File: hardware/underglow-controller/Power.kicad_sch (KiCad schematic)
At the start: 12 parts, among them U6 BD33C0AWFP-CE2

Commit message: almost done picking components i think
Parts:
- added D5: RB496EA, Package_TO_SOT_SMD:SOT-23-5, symbol ConeCodes:RB496EA
- gave numbers to parts that had none: 1
- renumbered C58 to C57, C57 to C58, R44 to R42, R40 to R43, R41 to R44, R42 to R45, R43 to R46
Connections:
- net IGNITION: now also D5.1 (A), D5.5 (K)
- net VBATT: now also D5.3 (A), D5.4 (K)
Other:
- moved on the sheet: D6
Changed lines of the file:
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@@
   (junction (at 57.15 76.2) (diameter 0) (color 0 0 0 0)
   )
-  (junction (at 35.56 76.2) (diameter 0) (color 0 0 0 0)
+  (junction (at 37.465 76.2) (diameter 0) (color 0 0 0 0)
   )
   (junction (at 81.915 77.47) (diameter 0) (color 0 0 0 0)
@@
     (stroke (width 0) (type default) (color 0 0 0 0))
   )
-  (wire (pts (xy 29.21 76.2) (xy 35.56 76.2))
+  (wire (pts (xy 33.02 76.2) (xy 37.465 76.2))
     (stroke (width 0) (type default) (color 0 0 0 0))
   )
@@
     (stroke (width 0) (type default) (color 0 0 0 0))
   )
-  (wire (pts (xy 35.56 76.2) (xy 57.15 76.2))
-    (stroke (width 0) (type default) (color 0 0 0 0))
-  )
   (wire (pts (xy 64.77 77.47) (xy 81.915 77.47))
     (stroke (width 0) (type default) (color 0 0 0 0))
@@
     (stroke (width 0) (type default) (color 0 0 0 0))
   )
-  (wire (pts (xy 34.29 71.12) (xy 53.34 71.12))
+  (wire (pts (xy 33.02 71.12) (xy 53.34 71.12))
     (stroke (width 0) (type default) (color 0 0 0 0))
   )
@@
     (stroke (width 0) (type default) (color 0 0 0 0))
   )
-  (wire (pts (xy 35.56 81.28) (xy 35.56 83.82))
+  (wire (pts (xy 37.465 81.28) (xy 37.465 83.82))
     (stroke (width 0) (type default) (color 0 0 0 0))
   )
@@
   )
   (wire (pts (xy 99.695 77.47) (xy 107.95 77.47))
+    (stroke (width 0) (type default) (color 0 0 0 0))
+  )
+  (wire (pts (xy 37.465 76.2) (xy 57.15 76.2))
     (stroke (width 0) (type default) (color 0 0 0 0))
   )
@@
     (effects (font (size 1.27 1.27)) (justify left bottom))
   )
-  (hierarchical_label "IGNITION" (shape input) (at 34.29 71.12 180)
+  (hierarchical_label "IGNITION" (shape input) (at 22.86 71.12 180)
     (effects (font (size 1.27 1.27)) (justify right))
   )
@@
     (effects (font (size 1.27 1.27)) (justify left))
   )
-  (hierarchical_label "VBATT" (shape input) (at 29.21 76.2 180)
+  (hierarchical_label "VBATT" (shape input) (at 22.86 76.2 180)
     (effects (font (size 1.27 1.27)) (justify right))
   )
   (symbol (lib_id "power:GND") (at 90.17 69.215 0) (unit 1)
     (in_bom yes) (on_board yes) (fields_autoplaced)
-    (property "Reference" "#PWR075" (id 0) (at 90.17 75.565 0)
+    (property "Reference" "#PWR076" (id 0) (at 90.17 75.565 0)
       (effects (font (size 1.27 1.27)) hide)
     )
@@
   (symbol (lib_id "power:+3V3") (at 107.95 77.47 0) (unit 1)
     (in_bom yes) (on_board yes) (fields_autoplaced)
-    (property "Reference" "#PWR076" (id 0) (at 107.95 81.28 0)
+    (property "Reference" "#PWR077" (id 0) (at 107.95 81.28 0)
       (effects (font (size 1.27 1.27)) hide)
     )
@@
   (symbol (lib_id "power:GND") (at 134.62 29.845 270) (unit 1)
     (in_bom yes) (on_board yes) (fields_autoplaced)
-    (property "Reference" "#PWR077" (id 0) (at 128.27 29.845 0)
+    (property "Reference" "#PWR072" (id 0) (at 128.27 29.845 0)
       (effects (font (size 1.27 1.27)) hide)
     )
@@
   (symbol (lib_id "Device:R_Small") (at 212.09 34.29 0) (unit 1)
     (in_bom yes) (on_board yes)
-    (property "Reference" "R40" (id 0) (at 213.36 33.02 0)
+    (property "Reference" "R43" (id 0) (at 213.36 33.02 0)
       (effects (font (size 1.27 1.27)) (justify left))
     )
@@
   (symbol (lib_id "Device:C_Small") (at 57.15 78.74 180) (unit 1)
     (in_bom yes) (on_board yes)
-    (property "Reference" "C57" (id 0) (at 59.69 77.4635 0)
+    (property "Reference" "C58" (id 0) (at 59.69 77.4635 0)
       (effects (font (size 1.27 1.27)) (justify right))
     )
@@
     (pin "2")
   )
-  (symbol (lib_id "power:GND") (at 35.56 83.82 0) (unit 1)
-    (in_bom yes) (on_board yes) (fields_autoplaced)
-    (property "Reference" "#PWR?" (id 0) (at 35.56 90.17 0)
-      (effects (font (size 1.27 1.27)) hide)
-    )
-    (property "Value" "GND" (id 1) (at 35.56 88.9 0))
-    (property "Footprint" "" (id 2) (at 35.56 83.82 0)
-      (effects (font (size 1.27 1.27)) hide)
-    )
-    (property "Datasheet" "" (id 3) (at 35.56 83.82 0)
+  (symbol (lib_id "power:GND") (at 37.465 83.82 0) (unit 1)
+    (in_bom yes) (on_board yes) (fields_autoplaced)
+    (property "Reference" "#PWR078" (id 0) (at 37.465 90.17 0)
+      (effects (font (size 1.27 1.27)) hide)
+    )
+    (property "Value" "GND" (id 1) (at 37.465 88.9 0))
+    (property "Footprint" "" (id 2) (at 37.465 83.82 0)
+      (effects (font (size 1.27 1.27)) hide)
+    )
+    (property "Datasheet" "" (id 3) (at 37.465 83.82 0)
       (effects (font (size 1.27 1.27)) hide)
     )
@@
   (symbol (lib_id "Device:R_Small") (at 81.915 66.675 0) (unit 1)
     (in_bom yes) (on_board yes) (fields_autoplaced)
-    (property "Reference" "R42" (id 0) (at 83.82 65.4049 0)
+    (property "Reference" "R45" (id 0) (at 83.82 65.4049 0)
       (effects (font (size 1.27 1.27)) (justify left))
     )
@@
     (pin "6")
   )
+  (symbol (lib_id "ConeCodes:RB496EA") (at 27.94 66.04 0) (unit 1)
+    (in_bom yes) (on_board yes) (fields_autoplaced)
+    (property "Reference" "D5" (id 0) (at 27.94 60.325 0))
+    (property "Value" "RB496EA" (id 1) (at 27.94 62.865 0))
+    (property "Footprint" "Package_TO_SOT_SMD:SOT-23-5" (id 2) (at 27.94 62.23 0)
+      (effects (font (size 1.27 1.27)) hide)
+    )
+    (property "Datasheet" "" (id 3) (at 27.94 66.04 0)
+      (effects (font (size 1.27 1.27)) hide)
+    )
+    (property "MPN" "RB496EA" (id 4) (at 27.94 65.405 0))
+    (pin "1")
+    (pin "2")
+    (pin "3")
+    (pin "4")
+    (pin "5")
+  )
   (symbol (lib_id "power:GND") (at 57.15 83.82 0) (unit 1)
     (in_bom yes) (on_board yes) (fields_autoplaced)
-    (property "Reference" "#PWR074" (id 0) (at 57.15 90.17 0)
+    (property "Reference" "#PWR079" (id 0) (at 57.15 90.17 0)
       (effects (font (size 1.27 1.27)) hide)
     )
@@
   (symbol (lib_id "Device:C_Small") (at 64.77 71.12 0) (unit 1)
     (in_bom yes) (on_board yes)
-    (property "Reference" "C58" (id 0) (at 66.675 69.8562 0)
+    (property "Reference" "C57" (id 0) (at 66.675 69.8562 0)
       (effects (font (size 1.27 1.27)) (justify left))
     )
@@
   (symbol (lib_id "Device:R_Small") (at 151.13 29.845 270) (unit 1)
     (in_bom yes) (on_board yes)
-    (property "Reference" "R44" (id 0) (at 152.4 27.305 90)
+    (property "Reference" "R42" (id 0) (at 152.4 27.305 90)
       (effects (font (size 1.27 1.27)) (justify left))
     )
@@
   (symbol (lib_id "Device:R_Small") (at 212.09 43.815 0) (unit 1)
     (in_bom yes) (on_board yes)
-    (property "Reference" "R41" (id 0) (at 213.995 43.18 0)
+    (property "Reference" "R44" (id 0) (at 213.995 43.18 0)
       (effects (font (size 1.27 1.27)) (justify left))
     )
@@
     (pin "2")
   )
-  (symbol (lib_id "Device:D_Schottky_Small") (at 35.56 78.74 270) (unit 1)
-    (in_bom yes) (on_board yes) (fields_autoplaced)
-    (property "Reference" "D?" (id 0) (at 37.465 78.4859 90)
-      (effects (font (size 1.27 1.27)) (justify left))
-    )
-    (property "Value" "D_Schottky_Small" (id 1) (at 33.02 77.2161 90)
+  (symbol (lib_id "Device:D_Schottky_Small") (at 37.465 78.74 270) (unit 1)
+    (in_bom yes) (on_board yes) (fields_autoplaced)
+    (property "Reference" "D6" (id 0) (at 39.37 78.4859 90)
+      (effects (font (size 1.27 1.27)) (justify left))
+    )
+    (property "Value" "D_Schottky_Small" (id 1) (at 34.925 77.2161 90)
       (effects (font (size 1.27 1.27)) (justify right) hide)
     )
-    (property "Footprint" "Diode_SMD:D_SMA" (id 2) (at 35.56 78.74 90)
-      (effects (font (size 1.27 1.27)) hide)
-    )
-    (property "Datasheet" "~" (id 3) (at 35.56 78.74 90)
-      (effects (font (size 1.27 1.27)) hide)
-    )
-    (property "MPN" "BYS10-45HE3_A/H" (id 4) (at 35.56 78.74 0)
+    (property "Footprint" "Diode_SMD:D_SMA" (id 2) (at 37.465 78.74 90)
+      (effects (font (size 1.27 1.27)) hide)
+    )
+    (property "Datasheet" "~" (id 3) (at 37.465 78.74 90)
+      (effects (font (size 1.27 1.27)) hide)
+    )
+    (property "MPN" "BYS10-45HE3_A/H" (id 4) (at 37.465 78.74 0)
       (effects (font (size 1.27 1.27)) hide)
     )
@@
   (symbol (lib_id "power:GND") (at 212.09 46.355 0) (unit 1)
     (in_bom yes) (on_board yes)
-    (property "Reference" "#PWR072" (id 0) (at 212.09 52.705 0)
+    (property "Reference" "#PWR075" (id 0) (at 212.09 52.705 0)
       (effects (font (size 1.27 1.27)) hide)
     )
@@
   (symbol (lib_id "power:+3V3") (at 186.69 29.845 0) (unit 1)
     (in_bom yes) (on_board yes) (fields_autoplaced)
-    (property "Reference" "#PWR078" (id 0) (at 186.69 33.655 0)
+    (property "Reference" "#PWR073" (id 0) (at 186.69 33.655 0)
       (effects (font (size 1.27 1.27)) hide)
     )
@@
   (symbol (lib_id "power:GND") (at 60.96 34.29 180) (unit 1)
     (in_bom yes) (on_board yes) (fields_autoplaced)
-    (property "Reference" "#PWR073" (id 0) (at 60.96 27.94 0)
+    (property "Reference" "#PWR074" (id 0) (at 60.96 27.94 0)
       (effects (font (size 1.27 1.27)) hide)
     )
@@
   (symbol (lib_id "Device:R_Small") (at 90.17 66.675 0) (unit 1)
     (in_bom yes) (on_board yes) (fields_autoplaced)
-    (property "Reference" "R43" (id 0) (at 92.71 65.4049 0)
-      (effects (font (size 1.27 1.27)) (justify left))
-    )
+    (property "Reference" "R46" (id 0) (at 92.71 65.4049 0)
+      (effects (font (size 1.27 1.27)) (justify left))
+    )

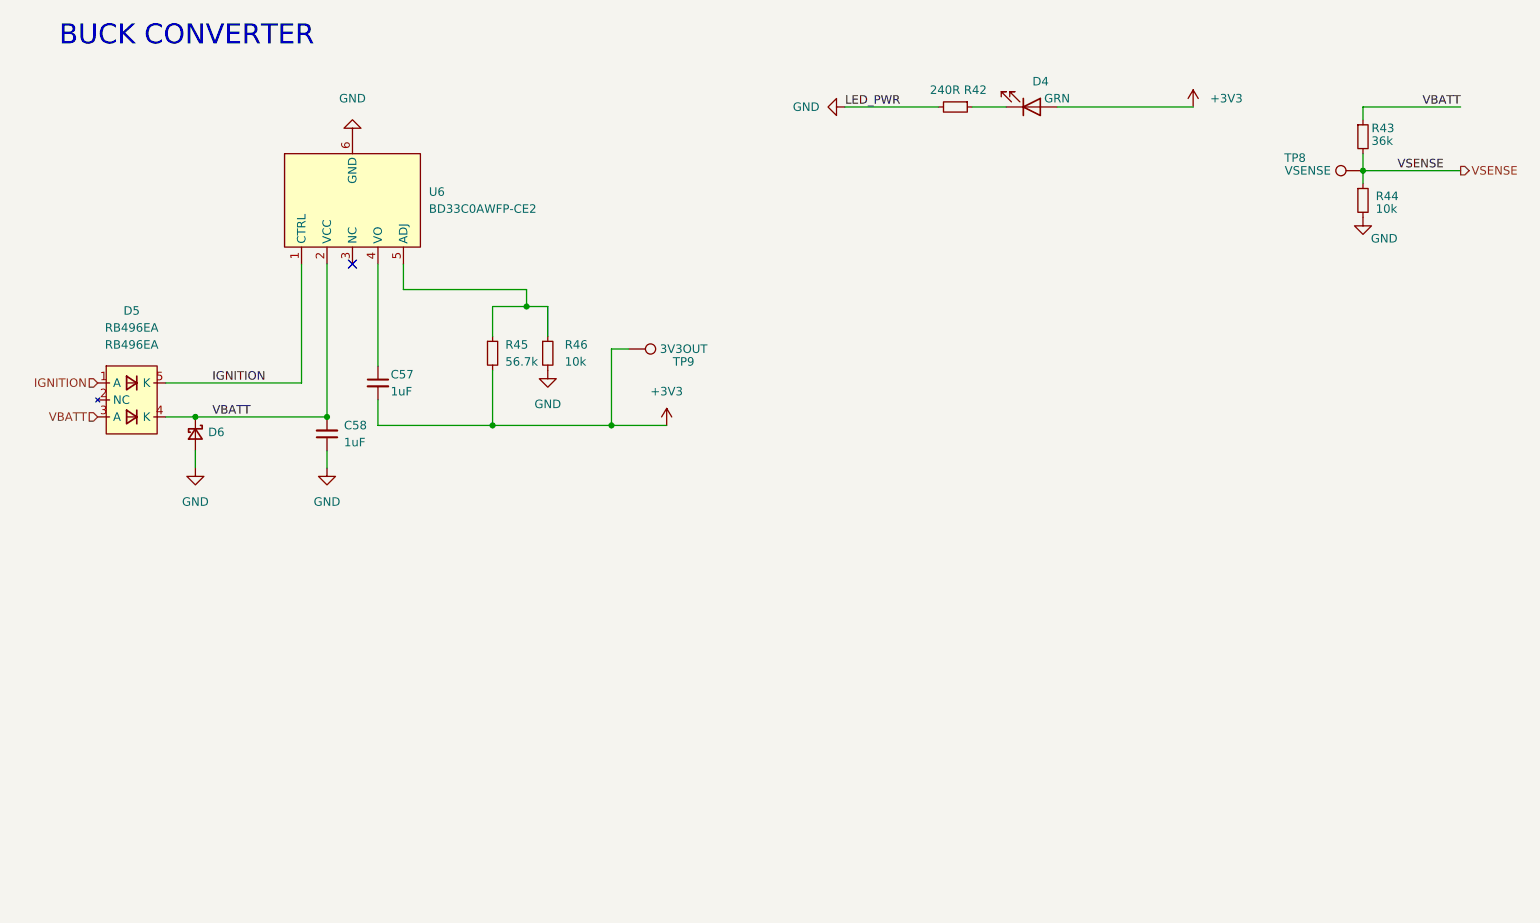
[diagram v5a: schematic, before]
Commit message: fix main sheet grid
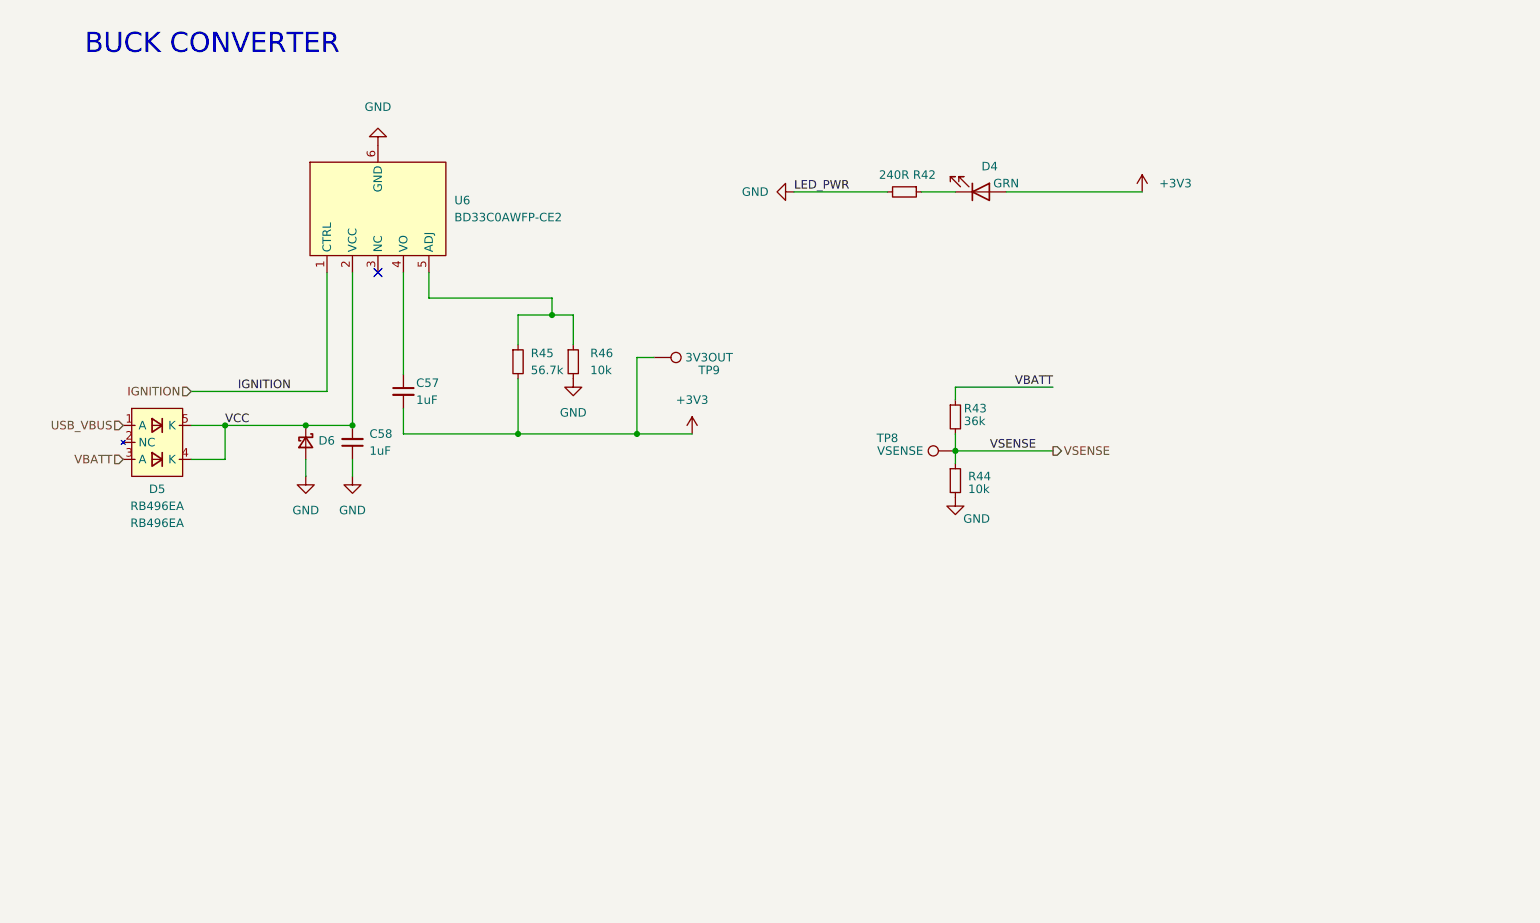
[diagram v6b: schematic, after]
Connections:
- net IGNITION: no longer D5.1 (A), D5.5 (K)
- net VBATT: no longer C58.2, D5.4 (K), D6.1 (K), U6.2 (VCC)
- new net USB_VBUS: D5.1 (A)
- new net VCC: C58.2, D5.4 (K), D5.5 (K), D6.1 (K), U6.2 (VCC)
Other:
- moved on the sheet: C57, C58, D4, D5, D6, R42, R43, R44, R45, R46, TP8, TP9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
